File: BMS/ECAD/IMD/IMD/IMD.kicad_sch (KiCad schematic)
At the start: 0 parts

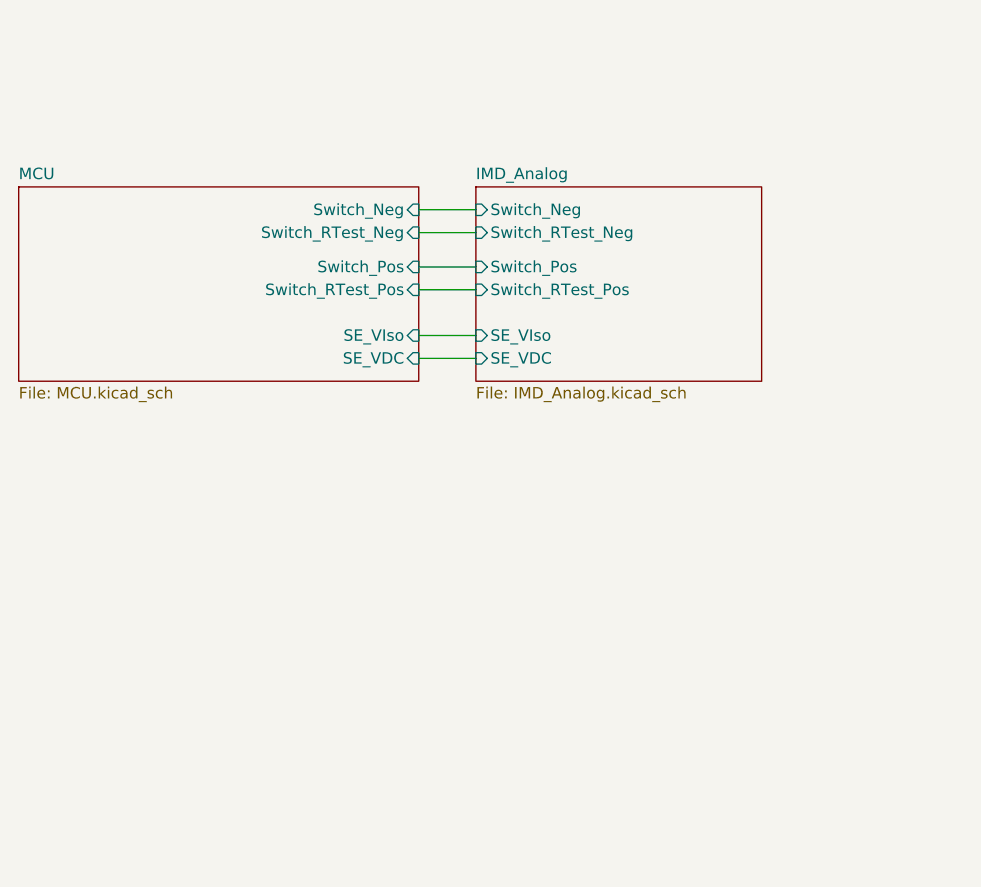
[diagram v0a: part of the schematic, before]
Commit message: add several subcomponent starts
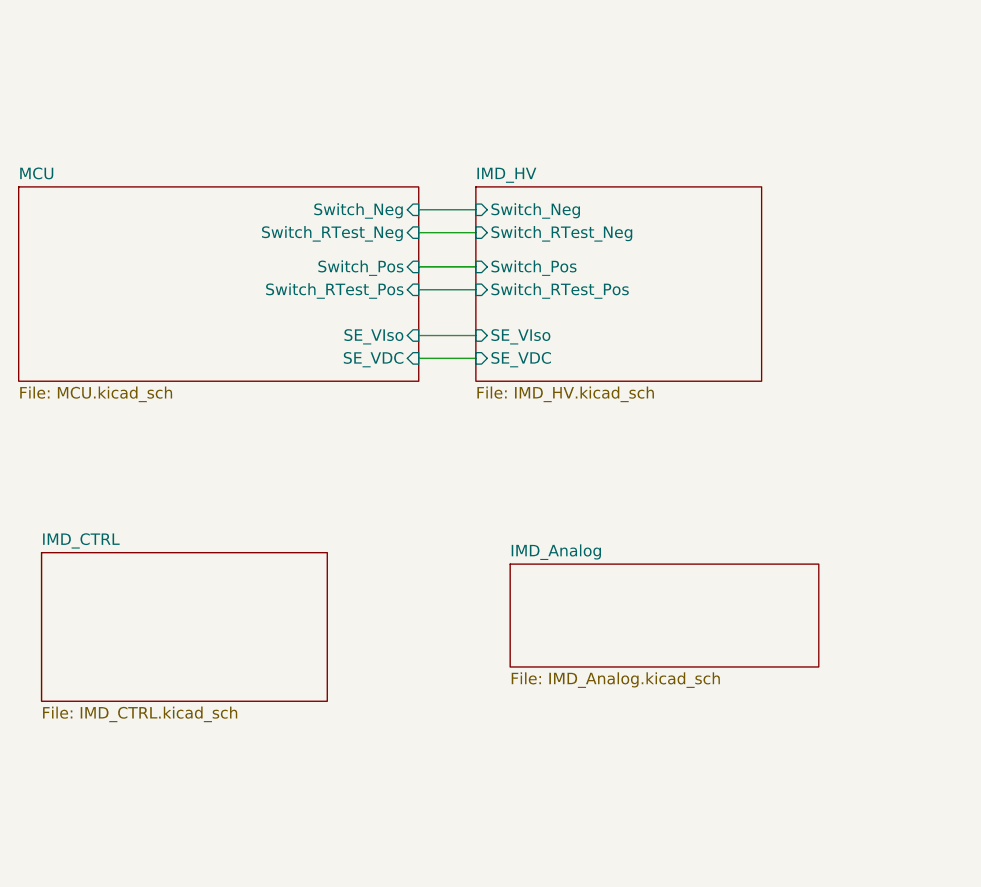
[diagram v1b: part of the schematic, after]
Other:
- added sheet IMD_CTRL (IMD_CTRL.kicad_sch)
- added sheet IMD_HV (IMD_HV.kicad_sch)
- sheet IMD_Analog ports: added none; removed SE_VDC, SE_VIso, Switch_Neg, Switch_Pos, Switch_RTest_Neg, Switch_RTest_Pos
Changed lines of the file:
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@@
+	)
+	(sheet
+		(at 217.17 187.96)
+		(size 34.29 11.43)
+		(exclude_from_sim no)
+		(in_bom yes)
+		(on_board yes)
+		(dnp no)
+		(fields_autoplaced yes)
+		(stroke
+			(width 0.1524)
+			(type solid)
+		)
+		(fill
+			(color 0 0 0 0.0000)
+		)
+		(property "Sheetname" "IMD_Analog"
+			(at 217.17 187.2484 0)
+			(effects
+				(font
+					(size 1.27 1.27)
+				)
+				(justify left bottom)
+			)
+		)
+		(property "Sheetfile" "IMD_Analog.kicad_sch"
+			(at 217.17 199.9746 0)
+			(effects
+				(font
+					(size 1.27 1.27)
+				)
+				(justify left top)
+			)
+		)
+		(instances
+			(project "IMD"
+				(path "/fb588915-3862-4dbd-8b18-9f4897ee9cfe"
+					(page "5")
+				)
+			)
+		)
 	)
 	(sheet
@@
 	)
 	(sheet
+		(at 165.1 186.69)
+		(size 31.75 16.51)
+		(exclude_from_sim no)
+		(in_bom yes)
+		(on_board yes)
+		(dnp no)
+		(fields_autoplaced yes)
+		(stroke
+			(width 0.1524)
+			(type solid)
+		)
+		(fill
+			(color 0 0 0 0.0000)
+		)
+		(property "Sheetname" "IMD_CTRL"
+			(at 165.1 185.9784 0)
+			(effects
+				(font
+					(size 1.27 1.27)
+				)
+				(justify left bottom)
+			)
+		)
+		(property "Sheetfile" "IMD_CTRL.kicad_sch"
+			(at 165.1 203.7846 0)
+			(effects
+				(font
+					(size 1.27 1.27)
+				)
+				(justify left top)
+			)
+		)
+		(instances
+			(project "IMD"
+				(path "/fb588915-3862-4dbd-8b18-9f4897ee9cfe"
+					(page "4")
+				)
+			)
+		)
+	)
+	(sheet
 		(at 213.36 146.05)
 		(size 31.75 21.59)
@@
 			(color 0 0 0 0.0000)
 		)
-		(property "Sheetname" "IMD_Analog"
+		(property "Sheetname" "IMD_HV"
 			(at 213.36 145.3384 0)
 			(effects
@@
 			)
 		)
-		(property "Sheetfile" "IMD_Analog.kicad_sch"
+		(property "Sheetfile" "IMD_HV.kicad_sch"
 			(at 213.36 168.2246 0)
 			(effects
